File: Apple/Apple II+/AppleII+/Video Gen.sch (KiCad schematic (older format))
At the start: 22 parts, among them Q3 2N3904

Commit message: updated additional sheets, and Readme.md
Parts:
- removed U?: 74LS51, symbol 74xx:74LS166
- added A10, B4, B9: 74LS194, symbol 74xx:74LS194
- added A11, B10: 74LS74, symbol 74xx:74LS74
- added unit 4 of A12
- added unit 3 of A12
- added A3: 74LS166, symbol 74xx:74LS166
- added A8: 74LS257, symbol 74xx:74LS257
- added unit 2 of B11
- added unit 4 of B11
- added unit 2 of B12
- added unit 4 of B13
- added unit 2 of B13
- added B2: 74LS86, symbol 74xx:74LS86
- added B3: 555, digikey-footprints:DIP-8_W7.62mm, symbol AppleII+:555_alt1
- added B5, B8: 74LS174, symbol AppleII+:74LS174
- added C13, C15: 0.1uf, symbol Device:C_Small
- added unit 1 of C14
- added C2: 47pf, symbol Device:C_Small
- added C3: 5-50pf, symbol Device:CTRIM_Small
- added J14B: Aux Video, symbol Connector_Generic:Conn_01x04
- added K14: VIDEO OUT, symbol Connector:Conn_Coaxial_Power
- added L1: 27uH, symbol Device:L
- added R10: 27R, symbol Device:R
- added R11: 200R, symbol Device:R_POT_TRIM_US
- added R12: 12K, symbol Device:R
- added R13: 3M3, symbol Device:R
- added R27: 4K7, symbol Device:R
- added R5: 1K, symbol Device:R
- added TP: Wire wrap post, symbol Connector:TestPoint
- B11: value 74LS51 -> 74LS08
- B12: value 74LS51 -> 74LS11
- gave numbers to parts that had none: 2
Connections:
- net R5 is gone; now on an unnamed net: R6.2
- net +5V: now also R9.1, B3.4 (RESET), B3.8 (VCC), R12.2; no longer R9.2
- net V2: now also B12.3
- net V4: now also B12.4
- net at B12.12: now also R5.1
- net GND: now reaches Q6.1 (E)
- net GND: now also A11.4 (~S), B3.1 (GND), C13.1, C14.1, C15.1, C2.2, C3.2, J14B.4 (Pin_4), K14.2 (Ext), L1.2, R11.3
- net at Q6.2 (C): now also C2.1, C3.1, L1.1, R5.2
- net at Q6.3 (B): now also R6.1, R27.1
- net at Q3.3 (B), R7.1, R8.1: no longer R6.1
- net at Q3.1 (E): now also J14B.3 (Pin_3), R11.1
- net at Q3.2 (C): now also R9.2; no longer R9.1
- new net: B12.6, B13.11
- new net: B13.13, B5.3 (1D)
- new net: B8.15 (3Q), B8.3 (1D)
- new net: A12.8, A12.9, B11.5, B8.2 (1Q)
- new net: A3.1 (Ds), B2.12
- new net: A3.13 (Qh), B2.13
- new net: A3.2 (A), B13.4
- new net: A12.10, A12.11
- new net: A11.1 (~R), A12.13
- new net: B11.11, B13.5
- new net: B11.13, B3.3 (OUT)
- new net: A11.6 (~Q), A8.1 (S)
- new net: R10.1, R11.2, TP.1
- new net: K14.1 (In), R10.2
- new net: B3.2 (TRIG), B3.6 (THRES), C15.2, R13.1
- new net: B3.7 (DISCH), R12.1, R13.2
- new net +12V: C14.2, J14B.1 (Pin_1)
- new net -5V: C13.2, J14B.2 (Pin_2)
- new net B5-2: B5.2 (1Q), B8.14 (3D)
- new net HIRES: B11.6
- new net LD6: B11.12
- new net SOFT5: A11.2 (D), A11.3 (C)
- new net SS-GR_~TXT: B13.12, R27.2
- new net SS-HI_~LORES: A12.12, B11.4
- new net SS-Mix_~NoMix: B12.5
- new net ~RAS: B5.9 (CLK), B8.9 (CLK), B8.9 (CLK)
- no-connect marks 0 -> 2
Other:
- moved on the sheet: A12B, A9, B11C, B12A, B13A, B14A, B14B, B14C, B14D, C13A, C13B, C14B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

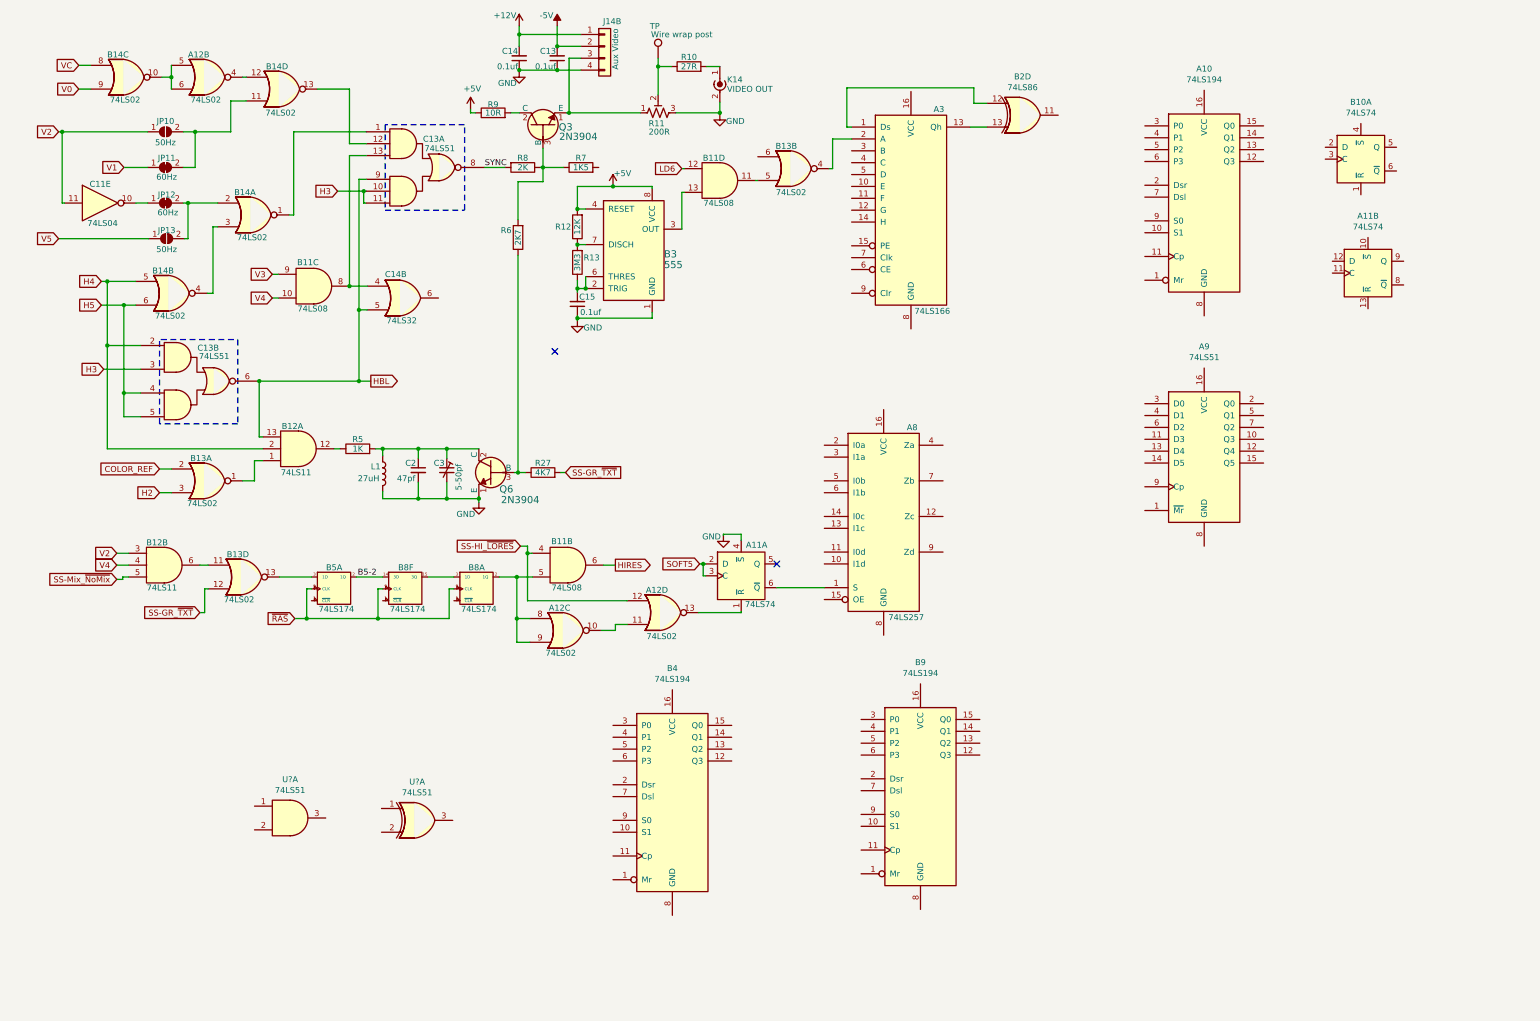
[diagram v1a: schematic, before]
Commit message: Draft final - finished video generation sheet and corrected IO Decode sheet
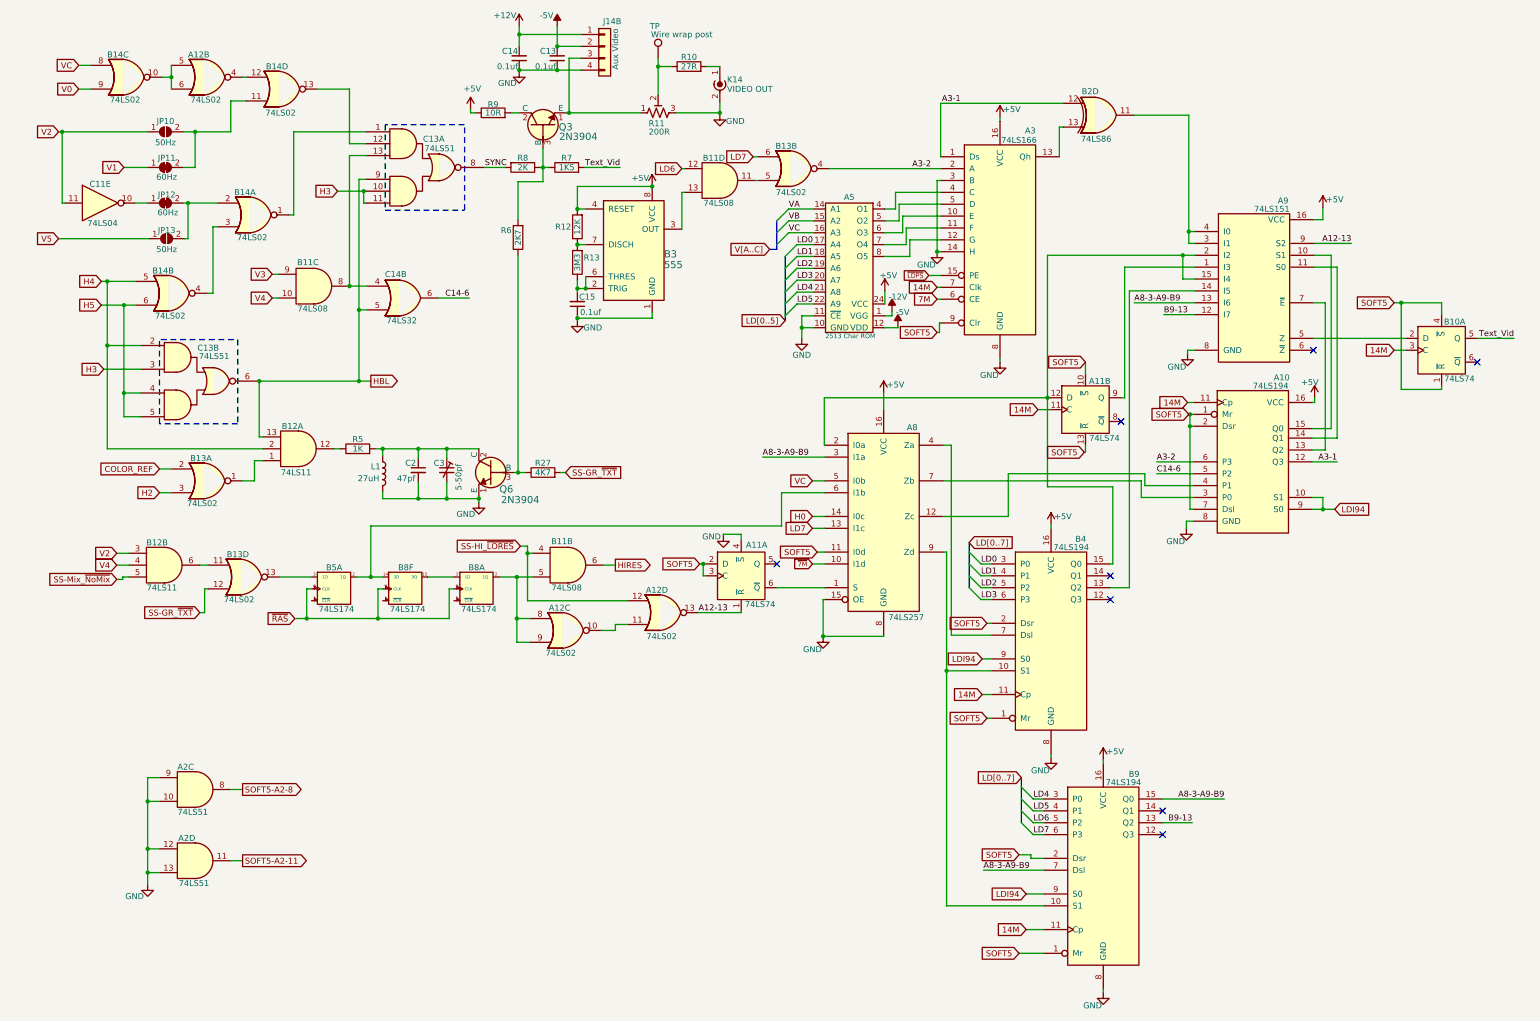
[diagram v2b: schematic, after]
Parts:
- removed A10: 74LS194, symbol 74xx:74LS194
- removed A9: 74LS51, symbol 74xx:74LS174
- removed U?: 74LS51, symbol 74xx:74LS86
- added A10: 74LS194, symbol AppleII+:74LS194
- added unit 4 of A2
- added A5: 2513 Char ROM, symbol AppleII+:2513
- added A9: 74LS151, symbol AppleII+:74LS151
- gave numbers to parts that had none: 1
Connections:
- net B5-2 is gone; now on an unnamed net: B5.2 (1Q), B8.14 (3D)
- net +5V: now also A3.16 (VCC), A8.16 (VCC), B4.16 (VCC), B9.16 (VCC), A10.16 (VCC), A5.24 (VCC), A9.16 (VCC)
- net -5V: now also A5.12 (VDD)
- net GND: now also A2.10, A2.9, A3.14 (H), A3.3 (B), A3.8 (GND), A8.15 (OE), A8.8 (GND), B4.8 (GND), B9.8 (GND), A10.8 (GND), A2.12, A2.13, A5.10 (GND), A5.11 (~CE), A9.8 (GND)
- net LD6: now also B9.5 (P2)
- net SOFT5: now also A11.10 (~S), A11.13 (~R), A3.9 (Clr), A8.11 (I0d), B10.1 (~R), B10.4 (~S), B4.1 (Mr), B4.2 (Dsr), B9.1 (Mr), B9.2 (Dsr), A10.1 (Mr), A10.2 (Dsr), A10.7 (Dsl)
- net VC: now also A8.5 (I0b), A5.16 (A3)
- net A3-1: now reaches A3.1 (Ds), B2.12
- net A3-1: now also A10.12 (Q3)
- net at A3.10 (E): now also A5.6 (O3)
- net at A3.11 (F): now also A5.7 (O4)
- net at A3.12 (G): now also A5.8 (O5)
- net ~LDPS: now reaches A3.15 (PE)
- net A3-2: now reaches A3.2 (A), B13.4
- net A3-2: now also A10.6 (P3)
- net at A3.4 (C): now also A5.4 (O1)
- net at A3.5 (D): now also A5.5 (O2)
- net 7M: now reaches A3.6 (CE)
- net 14M: now reaches A3.7 (Clk)
- net 14M: now also A11.11 (C), B10.3 (C), B4.11 (Cp), B9.11 (Cp), A10.11 (Cp)
- net A12-13: now reaches A11.1 (~R), A12.13
- net A12-13: now also A9.9 (S2)
- net LD7: now reaches B13.6
- net LD7: now also A8.13 (I1c), B9.6 (P3)
- net at B2.11: now also A9.3 (I1), A9.4 (I0)
- net ~7M: now reaches A8.10 (I1d)
- net at A8.12 (Zc): now also A10.4 (P1)
- net H0: now reaches A8.14 (I0c)
- net at A8.2 (I0a): now also A11.12 (D), B4.15 (Q0), A9.15 (I4), A9.2 (I2)
- net A8-3-A9-B9: now reaches A8.3 (I1a)
- net A8-3-A9-B9: now also B9.15 (Q0), B9.7 (Dsl), A9.13 (I6)
- net at A8.4 (Za): now also B4.7 (Dsl)
- net at A8.7 (Zb): now also A10.3 (P0)
- net at A8.9 (Zd): now also B4.10 (S1), B9.10 (S1)
- net at B10.2 (D): now also A9.5 (Z)
- net Text_Vid: now reaches B10.5 (Q)
- net Text_Vid: now also R7.2
- net at A11.9 (Q): now also A9.1 (I3)
- net at B4.13 (Q2): now also A9.14 (I5)
- net LD0: now reaches B4.3 (P0)
- net LD0: now also A5.17 (A4)
- net LD1: now reaches B4.4 (P1)
- net LD1: now also A5.18 (A5)
- net LD2: now reaches B4.5 (P2)
- net LD2: now also A5.19 (A6)
- net LD3: now reaches B4.6 (P3)
- net LD3: now also A5.20 (A7)
- net LDI94: now reaches B4.9 (S0)
- net LDI94: now also B9.9 (S0), A10.10 (S1), A10.9 (S0)
- net B9-13: now reaches B9.13 (Q2)
- net B9-13: now also A9.12 (I7)
- net LD4: now reaches B9.3 (P0)
- net LD4: now also A5.21 (A8)
- net LD5: now reaches B9.4 (P1)
- net LD5: now also A5.22 (A9)
- net C14-6: now reaches C14.6
- net C14-6: now also A10.5 (P2)
- new net: A10.15 (Q0), A9.10 (S1)
- new net: A10.14 (Q1), A9.11 (S0)
- new net: A10.13 (Q2), A9.7 (~E)
- new net -12V: A5.1 (VGG)
- new net SOFT5-A2-11: A2.11
- new net SOFT5-A2-8: A2.8
- new net VA: A5.14 (A1)
- new net VB: A5.15 (A2)
- no-connect marks 2 -> 8
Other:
- moved on the sheet: A11B, A3, B10A, B2D, B4, B9, R7
